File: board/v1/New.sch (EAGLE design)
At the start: 28 parts, among them IC2 LTC3525, IC3 MCP1703CB, U3 ATMEGA32U4, X1 USB-MICROB, Y1 8MHz

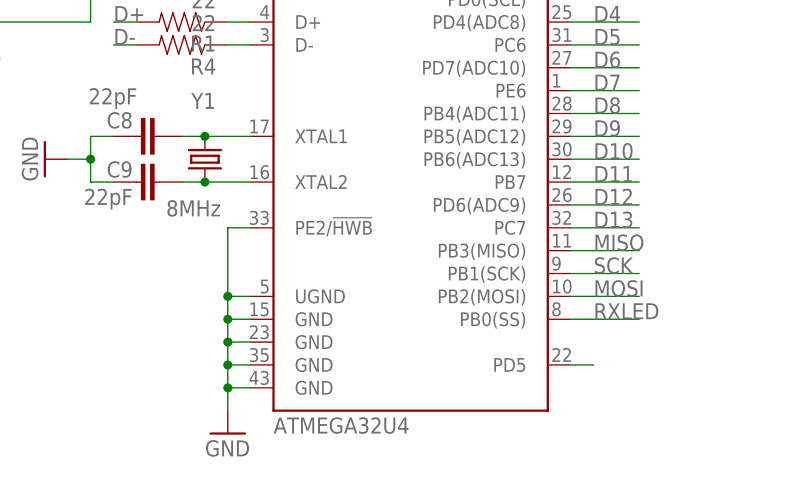
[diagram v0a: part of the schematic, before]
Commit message: Revert "example"
This reverts commit 1f9ad8d22b45befcb35b8a9bb4ed2c9c1b9cff3c.
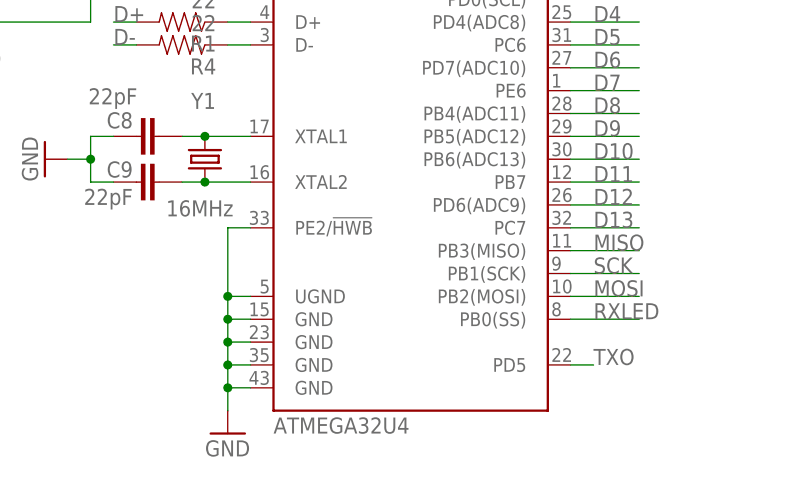
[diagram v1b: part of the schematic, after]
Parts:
- Y1: value 8MHz -> 16MHz
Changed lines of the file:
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@@
 <part name="GND13" library="SparkFun" deviceset="GND" device=""/>
 <part name="U3" library="SparkFun" deviceset="ATMEGA32U4" device="QFN2" value="ATMEGA32U4"/>
-<part name="Y1" library="SparkFun" deviceset="CRYSTAL" device="5X3" value="8MHz"/>
+<part name="Y1" library="SparkFun" deviceset="CRYSTAL" device="5X3" value="16MHz"/>
 <part name="C8" library="SparkFun" deviceset="CAP" device="0402-CAP" value="22pF"/>
 <part name="C9" library="SparkFun" deviceset="CAP" device="0402-CAP" value="22pF"/>
@@
 <wire x1="83.82" y1="10.16" x2="83.82" y2="5.08" width="0.1524" layer="91"/>
 <pinref part="R6" gate="G$1" pin="1"/>
+<label x="50.8" y="-12.7" size="1.778" layer="95"/>
 <label x="76.2" y="10.16" size="1.778" layer="95"/>
 </segment>
